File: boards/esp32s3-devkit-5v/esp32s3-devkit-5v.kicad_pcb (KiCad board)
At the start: 4 copper layers, 59.3 x 38 mm, 37 parts, among them J1 Conn_01x17_Pin, J2 Conn_01x17_Pin, J3 USB_C_Receptacle_USB2.0_16P, Q1 AO3401A, SW1 MK-12C03-G015, SW2 RESET, SW3 BOOT, U1 TPS63070RNMR, U2 ESP32-S3-WROOM-1-N16, U3 USBLC6-2SC6

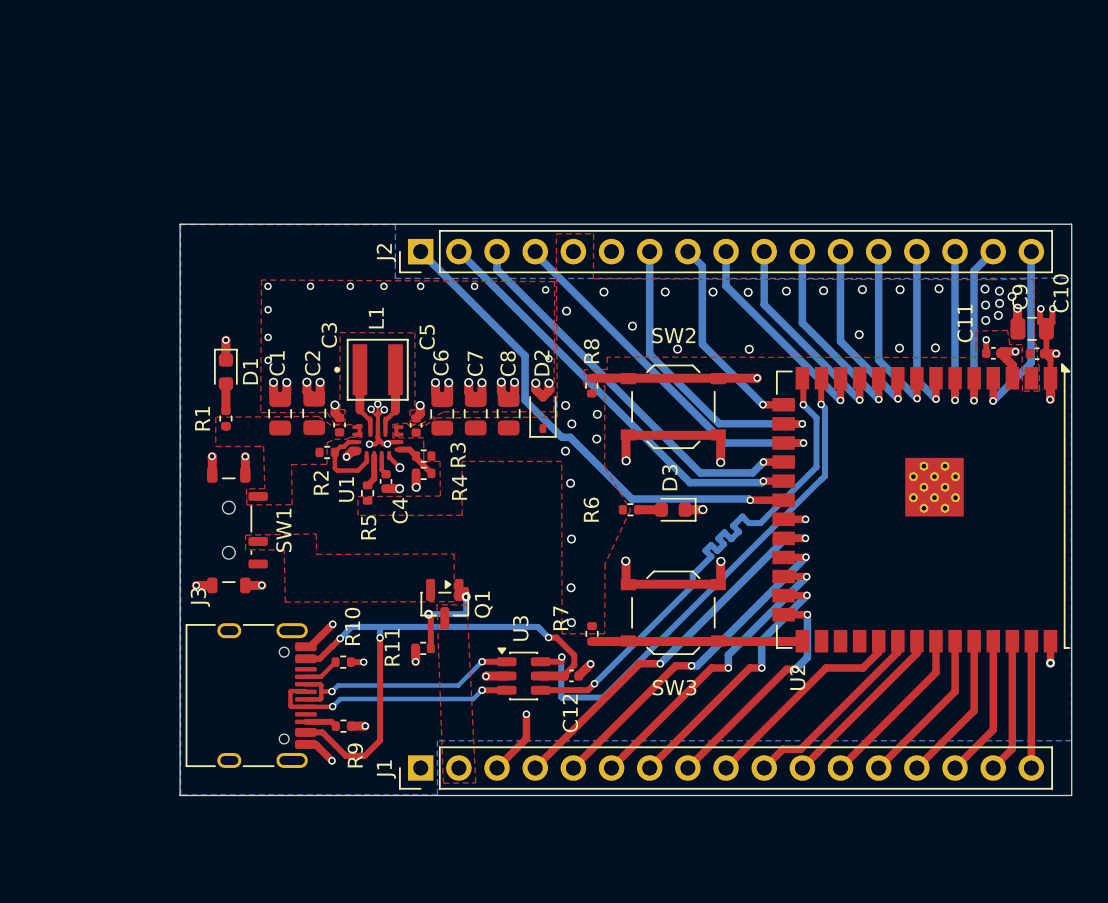
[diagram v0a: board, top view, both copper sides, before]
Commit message: feat(esp32s3-devkit-5v): add compact dual-rail PCB and physical screening (#122)
* feat(esp32s3-devkit-5v): add reviewed schematic and routed prototype

* Compact dual-rail PCB and add safe power monitoring

* fix(pcb): restore close converter bypass placement and guard it

* test(pcb): add physical screening and compact-layout test report

* fix(ci): build FastHenry with portable scalar compiler settings

* fix(ci): rebuild cached FastHenry objects with selected flags

* fix(sim): repair FastHenry sparse statistics adapter pointer

* test(pcb): model three-AA power limits and define bench validation

* test(audio): screen continuous alarm loads and document speaker proposal

* docs(audio): define bedroom wake-up validation and refresh evidence
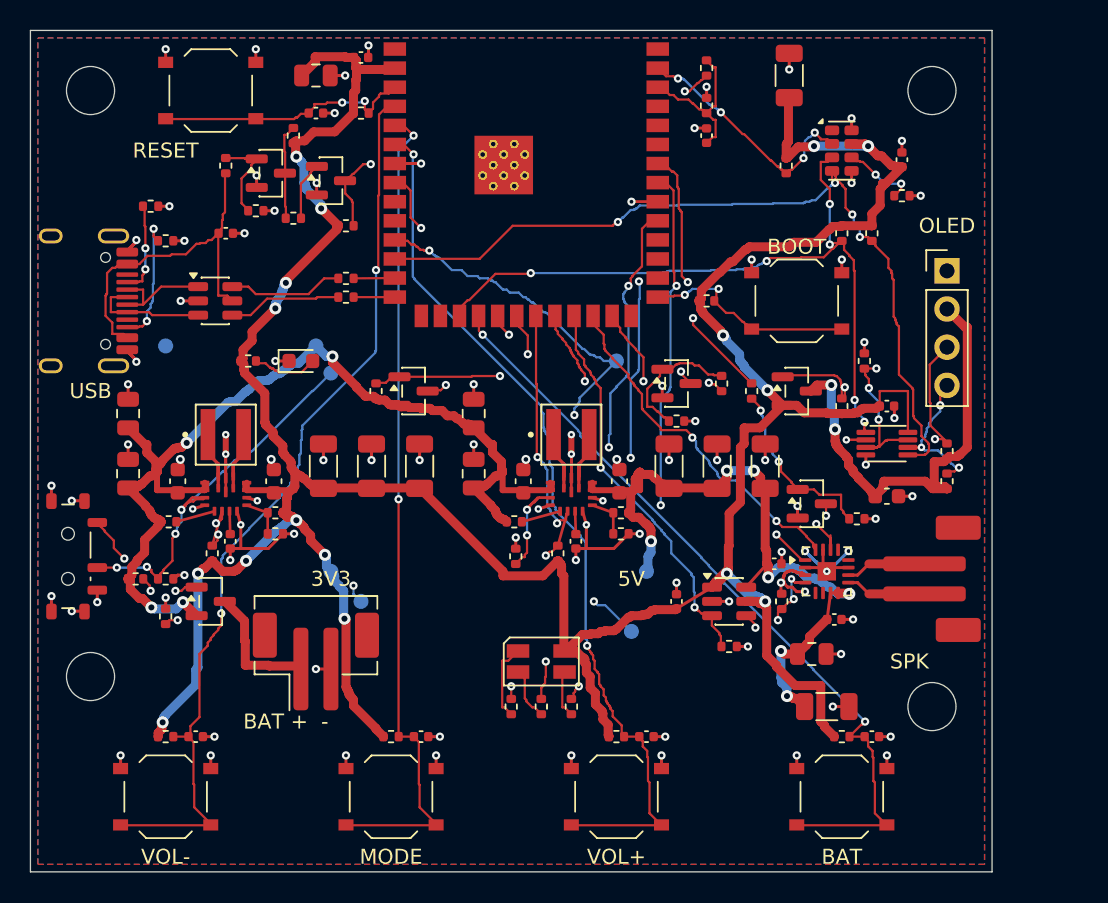
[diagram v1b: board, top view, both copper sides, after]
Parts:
- removed D3: LED, LED_SMD:LED_0603_1608Metric
- removed R2: 10kΩ, Resistor_SMD:R_0402_1005Metric
- added C13: 10µF, Capacitor_SMD:C_0603_1608Metric, F.Cu at (139.2, 100.0)
- added C14: 22µF, Capacitor_SMD:C_1206_3216Metric, F.Cu at (142.5, 99.0)
- added C15: 22µF, Capacitor_SMD:C_1206_3216Metric, F.Cu at (145.7, 99.0)
- added C16: 22µF, Capacitor_SMD:C_1206_3216Metric, F.Cu at (148.9, 99.0)
- added C17: 22µF, Capacitor_SMD:C_0805_2012Metric, F.Cu at (119.0, 73.0)
- added C18: 0.1µF, Capacitor_SMD:C_0402_1005Metric, F.Cu at (122.0, 71.8)
- added C19: 1µF, Capacitor_SMD:C_0402_1005Metric, F.Cu at (119.0, 75.5)
- added C20: 0.1µF, Capacitor_SMD:C_0402_1005Metric, F.Cu at (113.0, 83.5)
- added C21: 100µF, Capacitor_SMD:C_1206_3216Metric, F.Cu at (150.5, 73.0)
- added C22: 0.1µF, Capacitor_SMD:C_0402_1005Metric, F.Cu at (111.0, 117.0)
- added C23: 0.1µF, Capacitor_SMD:C_0402_1005Metric, F.Cu at (126.0, 117.0)
- added C24: 0.1µF, Capacitor_SMD:C_0402_1005Metric, F.Cu at (141.0, 117.0)
- added C25: 0.1µF, Capacitor_SMD:C_0402_1005Metric, F.Cu at (156.0, 117.0)
- added C26: 100µF, Capacitor_SMD:C_1206_3216Metric, F.Cu at (153.0, 115.0)
- added C27: 10µF, Capacitor_SMD:C_0805_2012Metric, F.Cu at (152.0, 111.5)
- added C28: 0.1µF, Capacitor_SMD:C_0402_1005Metric, F.Cu at (153.5, 109.2)
- added C29: 0.1µF, Capacitor_SMD:C_0402_1005Metric, F.Cu at (158.0, 78.6)
- added C30: 0.1µF, Capacitor_SMD:C_0402_1005Metric, F.Cu at (157.0, 95.0)
- added C31: 1µF, Capacitor_SMD:C_0603_1608Metric, F.Cu at (157.0, 101.0)
- added C32: 0.1µF, Capacitor_SMD:C_0402_1005Metric, F.Cu at (143.0, 108.0)
- added C33: 0.1µF, Capacitor_SMD:C_0402_1005Metric, F.Cu at (149.5, 105.5)
- added C34: 0.1uF, Capacitor_SMD:C_0402_1005Metric, F.Cu at (145.0, 77.0)
- added H1: M3, MountingHole_3.2mm_M3, F.Cu at (104.0, 74.0)
- added H2: M3, MountingHole_3.2mm_M3, F.Cu at (160.0, 74.0)
- added H3: M3, MountingHole_3.2mm_M3, F.Cu at (104.0, 113.0)
- added H4: M3, MountingHole_3.2mm_M3, F.Cu at (160.0, 115.0)
- added J4: Conn_01x04_Pin, Connector_PinHeader_2.54mm:PinHeader_1x04_P2.54mm_Vertical, F.Cu at (161.0, 86.0)
- added L2: 1.5µH, TPS63070:IND_XFL4020-152MEC, F.Cu at (136.0, 96.9)
- added Q2: AO3401A, Package_TO_SOT_SMD:SOT-23, F.Cu at (151.0, 94.0)
- added Q3: MMBT3904, Package_TO_SOT_SMD:SOT-23, F.Cu at (152.0, 101.5)
- added Q4: MMBT3904, Package_TO_SOT_SMD:SOT-23, F.Cu at (116.0, 79.5)
- added Q5: MMBT3904, Package_TO_SOT_SMD:SOT-23, F.Cu at (120.0, 80.0)
- added Q6: AO3401A, Package_TO_SOT_SMD:SOT-23, F.Cu at (125.5, 94.0)
- added Q7: MMBT3904, Package_TO_SOT_SMD:SOT-23, F.Cu at (143.0, 93.5)
- added R12: 10kΩ, Resistor_SMD:R_0402_1005Metric, F.Cu at (145.0, 88.0)
- added R13: 10kΩ, Resistor_SMD:R_0402_1005Metric, F.Cu at (122.0, 75.5)
- added R14: 5.1kΩ, Resistor_SMD:R_0402_1005Metric, F.Cu at (109.0, 84.0)
- added R15: 5.1kΩ, Resistor_SMD:R_0402_1005Metric, F.Cu at (108.0, 81.7)
- added R16: 4.7kΩ, Resistor_SMD:R_0402_1005Metric, F.Cu at (154.0, 83.5)
- added R17: 4.7kΩ, Resistor_SMD:R_0402_1005Metric, F.Cu at (156.0, 83.5)
- added R18: 10kΩ, Resistor_SMD:R_0402_1005Metric, F.Cu at (150.3, 79.0)
- added R19: 100kΩ, Resistor_SMD:R_0402_1005Metric, F.Cu at (132.3, 105.0)
- added R20: 100kΩ, Resistor_SMD:R_0402_1005Metric, F.Cu at (150.0, 108.0)
- added R21: 100kΩ, Resistor_SMD:R_0402_1005Metric, F.Cu at (154.0, 95.0)
- added R22: 10kΩ, Resistor_SMD:R_0402_1005Metric, F.Cu at (148.0, 94.0)
- added R23: 100kΩ, Resistor_SMD:R_0402_1005Metric, F.Cu at (155.0, 102.5)
- added R24: 10kΩ, Resistor_SMD:R_0402_1005Metric, F.Cu at (109.0, 117.0)
- added R25: 10kΩ, Resistor_SMD:R_0402_1005Metric, F.Cu at (124.0, 117.0)
- added R26: 10kΩ, Resistor_SMD:R_0402_1005Metric, F.Cu at (139.0, 117.0)
- added R27: 10kΩ, Resistor_SMD:R_0402_1005Metric, F.Cu at (154.0, 117.0)
- added R28: 330Ω, Resistor_SMD:R_0402_1005Metric, F.Cu at (132.0, 115.0)
- added R29: 150Ω, Resistor_SMD:R_0402_1005Metric, F.Cu at (134.0, 115.0)
- added R30: 150Ω, Resistor_SMD:R_0402_1005Metric, F.Cu at (136.0, 115.0)
- added R31: 10kΩ, Resistor_SMD:R_0402_1005Metric, F.Cu at (107.0, 106.5)
- added R32: 100kΩ, Resistor_SMD:R_0402_1005Metric, F.Cu at (109.0, 106.5)
- added R33: 10kΩ, Resistor_SMD:R_0402_1005Metric, F.Cu at (158.0, 81.0)
- added R34: 22Ω, Resistor_SMD:R_0402_1005Metric, F.Cu at (121.0, 86.5)
- added R35: 22Ω, Resistor_SMD:R_0402_1005Metric, F.Cu at (121.0, 87.8)
- added R36: 100kΩ, Resistor_SMD:R_0402_1005Metric, F.Cu at (155.5, 92.0)
- added R37: 4.7kΩ, Resistor_SMD:R_0402_1005Metric, F.Cu at (161.0, 98.0)
- added R38: 4.7kΩ, Resistor_SMD:R_0402_1005Metric, F.Cu at (161.0, 100.0)
- added R39: 100kΩ, Resistor_SMD:R_0402_1005Metric, F.Cu at (146.5, 111.0)
- added R40: 100k, Resistor_SMD:R_0402_1005Metric, F.Cu at (113.0, 79.0)
- added R41: 1M, Resistor_SMD:R_0402_1005Metric, F.Cu at (115.0, 82.0)
- added R42: 47k, Resistor_SMD:R_0402_1005Metric, F.Cu at (117.5, 77.0)
- added R43: 10k, Resistor_SMD:R_0402_1005Metric, F.Cu at (117.5, 82.5)
- added R44: 47k, Resistor_SMD:R_0402_1005Metric, F.Cu at (121.0, 83.0)
- added R45: 100k, Resistor_SMD:R_0402_1005Metric, F.Cu at (123.0, 94.0)
- added R46: 10k, Resistor_SMD:R_0402_1005Metric, F.Cu at (146.0, 93.5)
- added R47: 100k, Resistor_SMD:R_0402_1005Metric, F.Cu at (143.0, 96.0)
- added R48: 33k, Resistor_SMD:R_0402_1005Metric, F.Cu at (145.0, 72.5)
- added R49: 10k, Resistor_SMD:R_0402_1005Metric, F.Cu at (145.0, 75.0)
- added SW4: VOL-, Button_Switch_SMD:SW_Push_1P1T_XKB_TS-1187A, F.Cu at (109.0, 121.0)
- added SW5: MODE, Button_Switch_SMD:SW_Push_1P1T_XKB_TS-1187A, F.Cu at (124.0, 121.0)
- added SW6: VOL+, Button_Switch_SMD:SW_Push_1P1T_XKB_TS-1187A, F.Cu at (139.0, 121.0)
- added SW7: BATTERY, Button_Switch_SMD:SW_Push_1P1T_XKB_TS-1187A, F.Cu at (154.0, 121.0)
- added TP1: GND, TestPoint_Pad_D1.0mm, B.Cu at (109.0, 91.0)
- added TP2: PFET, TestPoint_Pad_D1.0mm, B.Cu at (119.0, 91.0)
- added TP3: 3v3, TestPoint_Pad_D1.0mm, B.Cu at (120.0, 106.0)
- added TP4: 5v, TestPoint_Pad_D1.0mm, B.Cu at (141.0, 106.0)
- added TP5: GPIO15, TestPoint_Pad_D1.0mm, B.Cu at (122.0, 108.0)
- added TP6: GPIO13, TestPoint_Pad_D1.0mm, B.Cu at (140.0, 110.0)
- added TP7: EN_3V3, TestPoint_Pad_D1.0mm, B.Cu at (120.0, 92.8)
- added TP8: GPIO18, TestPoint_Pad_D1.0mm, B.Cu at (139.0, 92.0)
- added U4: USBLC6-2SC6, Package_TO_SOT_SMD:SOT-23-6, F.Cu at (112.3, 88.0)
- added U5: RV-3028-C7, Package_SON:MicroCrystal_C7_SON-8_1.5x3.2mm_P0.9mm, F.Cu at (154.0, 78.0)
- added U6: MAX98357A, Package_DFN_QFN:TQFN-16-1EP_3x3mm_P0.5mm_EP1.23x1.23mm, F.Cu at (153.0, 106.0)
- added U7: SN74LVC2G66DCUR, Package_SO:VSSOP-8_2.3x2mm_P0.5mm, F.Cu at (157.0, 97.5)
- added U8: SN74LVC1T45DBVR, Package_TO_SOT_SMD:SOT-23-6, F.Cu at (146.5, 108.0)
- C10: value 0.1µF -> 10µF; footprint Capacitor_SMD:C_0402_1005Metric -> Capacitor_SMD:C_0805_2012Metric
- C11: value 1µF -> 10µF; footprint Capacitor_SMD:C_0402_1005Metric -> Capacitor_SMD:C_0603_1608Metric
- C3, C5: footprint Capacitor_SMD:C_0402_1005Metric -> Capacitor_SMD:C_0603_1608Metric
- C6, C7, C8: footprint Capacitor_SMD:C_0805_2012Metric -> Capacitor_SMD:C_1206_3216Metric
- C9: value 22µF -> 10µF
- D2: value 3.6v -> 150141M173100; footprint Diode_SMD:D_SOD-323 -> LED_SMD:LED_RGB_Wuerth-PLCC4_3.2x2.8mm_150141M173100
- J1: value Conn_01x17_Pin -> Conn_01x02_Pin; footprint Connector_PinHeader_2.54mm:PinHeader_1x17_P2.54mm_Vertical -> Connector_JST:JST_PH_B2B-PH-SM4-TB_1x02-1MP_P2.00mm_Vertical
- J2: value Conn_01x17_Pin -> USB_C_Receptacle_USB2.0_16P; footprint Connector_PinHeader_2.54mm:PinHeader_1x17_P2.54mm_Vertical -> Board:USB_C_HRO_Overhang
- J3: value USB_C_Receptacle_USB2.0_16P -> Conn_01x02_Pin; footprint Connector_USB:USB_C_Receptacle_HRO_TYPE-C-31-M-12 -> Board:JST_PH_Speaker_Overhang
- R1, R6: value 1kΩ -> 100kΩ
- R10: value 5.1kΩ -> 100kΩ
- R11: value 100kΩ -> 1kΩ
- R3: value 470kΩ -> 10kΩ
- R4: value 150kΩ -> 470kΩ
- R5: value 100kΩ -> 150kΩ
- R8: value 10kΩ -> 680kΩ
- R9: value 5.1kΩ -> 130kΩ
- SW1: value MK-12C03-G015 -> MSK12C02
- U2: value ESP32-S3-WROOM-1-N16 -> TPS63070RNMR; footprint RF_Module:ESP32-S3-WROOM-1 -> TPS63070:TPS63070
- U3: value USBLC6-2SC6 -> ESP32-S3-WROOM-1-N16; footprint Package_TO_SOT_SMD:SOT-23-6 -> Board:ESP32-S3-WROOM-1_Overhang
- moved J3 46.4 mm to (160.0, 106.5)
- moved C10 38.3 mm to (129.5, 99.5), turned to 90 degrees
- moved C9 37.6 mm to (129.5, 95.5), turned to 90 degrees
- moved SW2 37.3 mm to (112.0, 74.0), turned to 0 degrees
- moved U3 36.5 mm to (133.0, 76.5)
- moved C11 32.4 mm to (132.8, 100.0), turned to 90 degrees
- moved R6 28.0 mm to (112.1, 104.8), turned to 90 degrees
- moved U2 26.6 mm to (136.0, 102.0), turned to 0 degrees
- moved J2 23.8 mm to (102.4, 88.0), turned to -90 degrees
- moved R9 22.5 mm to (139.3, 103.5)
- moved R11 22.4 mm to (114.5, 92.0), turned to 0 degrees
- moved SW3 22.3 mm to (151.0, 88.0)
- moved R3 17.5 mm to (109.2, 102.7), turned to 0 degrees
- moved D2 16.6 mm to (134.0, 112.0), turned to 0 degrees
- moved R10 16.0 mm to (135.1, 104.8), turned to 90 degrees
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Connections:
- C1 pad 1: /VBAT_SW -> /PFET
- C10 pad 1: /3v3 -> /PFET
- C11 pad 1: Net-(U2-EN) -> /PFET
- C12 pad 1: Net-(U3-VBUS) -> Net-(U2-VAUX)
- C2 pad 1: /VBAT_SW -> /PFET
- C3 pad 1: /VBAT_SW -> /PFET
- C9 pad 1: /3v3 -> /PFET
- D2 pad 2: GND -> Net-(D2-BK)
- J1 pad 1: GND -> /VBAT
- J1 pad 2: /VBAT -> GND
- R1 pad 1: /VBAT_SW -> Net-(Q1-G)
- R1 pad 2: Net-(D1-A) -> GND
- R10 pad 1: Net-(J3-CC1) -> /3v3
- R10 pad 2: GND -> /GPIO13
- R11 pad 1: Net-(Q1-G) -> /3v3
- R11 pad 2: GND -> Net-(D1-A)
- R3 pad 1: /3v3 -> /PFET
- R3 pad 2: Net-(U1-FB) -> Net-(U1-PS_SYNC)
- R4 pad 1: Net-(U1-FB) -> /3v3
- R4 pad 2: GND -> Net-(U1-FB)
- R5 pad 1: /3v3 -> Net-(U1-FB)
- R5 pad 2: Net-(U1-PG) -> GND
- R6 pad 2: Net-(D3-A) -> /GPIO15
- R7 pad 1: /3v3 -> /PFET
- R7 pad 2: Net-(U2-IO0) -> Net-(U2-PS_SYNC)
- R8 pad 1: /3v3 -> /5v
- R8 pad 2: Net-(U2-EN) -> Net-(U2-FB)
- R9 pad 1: Net-(J3-CC2) -> Net-(U2-FB)
- SW1 pad 1: /VBAT_SW -> /SW_ON
- SW1 pad 2: /PFET -> /EN_3V3
- SW1 pad 3: unconnected-(SW1-C-Pad3) -> GND
- SW2 pad 2: Net-(U2-EN) -> Net-(U3-EN)
- SW3 pad 2: Net-(U2-IO0) -> Net-(U3-IO0)
- U1 pad 1: Net-(U1-EN) -> Net-(U1-PS_SYNC)
- U1 pad 12: /VBAT_SW -> /PFET
- U1 pad 13: /VBAT_SW -> /PFET
- U1 pad 14: Net-(U1-EN) -> /EN_3V3
- U1 pad 2: Net-(U1-PG) -> /GPIO15
- U2 pad 1: GND -> Net-(U2-PS_SYNC)
- U2 pad 10: /GPIO17 -> GND
- U2 pad 11: /GPIO18 -> Net-(U2-L1)
- U2 pad 12: /GPIO8 -> /PFET
- U2 pad 13: /D- -> /PFET
- U2 pad 14: /D+ -> /GPIO18
- U2 pad 15: /GPIO3 -> GND
- U2 pad 2: /3v3 -> /GPIO13
- U2 pad 3: Net-(U2-EN) -> Net-(U2-VAUX)
- U2 pad 4: /GPIO4 -> GND
- U2 pad 5: /GPIO5 -> Net-(U2-FB)
- U2 pad 6: /GPIO6 -> GND
- U2 pad 7: /GPIO7 -> /5v
- U2 pad 8: /GPIO15 -> /5v
- U2 pad 9: /GPIO16 -> Net-(U2-L2)
- U3 pad 1: Net-(J3-D--PadA7) -> GND
- U3 pad 2: GND -> /3v3
- U3 pad 3: Net-(J3-D+-PadA6) -> Net-(U3-EN)
- U3 pad 4: /D+ -> /GPIO4
- U3 pad 5: Net-(U3-VBUS) -> /GPIO5
- U3 pad 6: /D- -> /GPIO6
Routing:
- net /3v3: track 1.37 -> 227.0 mm, vias 33 -> 16
- net /PFET: track 0.00 -> 67.2 mm, vias 0 -> 4
- net /5v: track 0.00 -> 49.8 mm, vias 0 -> 7
- net /GPIO4: track 12.5 -> 61.6 mm, vias 1 -> 2
- net /GPIO6: track 11.4 -> 59.8 mm, vias 1 -> 2
- net /GPIO5: track 11.9 -> 55.6 mm, vias 1 -> 2
- net /GPIO8: track 14.5 -> 55.5 mm, vias 1 -> 4
- net GND: track 75.7 -> 114.1 mm, vias 57 -> 93
- net Net-(U3-VBUS): track 36.3 -> 0.00 mm, vias 3 -> 0
- net /GPIO15: track 12.2 -> 45.4 mm, vias 1 -> 4
- net Net-(U2-EN): track 32.0 -> 0.00 mm, vias 2 -> 0
- net /OLED_3V3: track 0.00 -> 30.8 mm, vias 0 -> 2
- net /Power monitoring/BAT_MEAS: track 0.00 -> 29.4 mm, vias 0 -> 2
- net /EN_3V3: track 0.00 -> 29.2 mm, vias 0 -> 4
- net /D+: track 34.7 -> 7.55 mm, vias 2 -> 0
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- added copper zone on In2.Cu, net GND
- removed copper zone on F.Cu, net /3v3
- removed copper zone on In2.Cu, net /3v3
- removed copper zone on F.Cu, net /PFET
- removed copper zone on F.Cu, net /VBAT
- removed copper zone on F.Cu, net /VBAT_SW
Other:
- board size 59.3 x 38 mm -> 64 x 56 mm
- board text added: "3V3"
- board text added: "5V"
- board text added: "BAT"
- board text added: "BAT + -"
- board text added: "BOOT"
- board text added: "MODE"
- board text added: "OLED"
- board text added: "RESET"
- board text added: "SPK"
- board text added: "USB"
- board text added: "VOL+"
- board text added: "VOL-"
